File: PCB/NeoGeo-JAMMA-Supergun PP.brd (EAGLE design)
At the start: 58.5 x 61 mm, 18 parts, among them U1A SN74AHCT125N, U2A SN74AHCT125N, U3A SN74AHCT125N

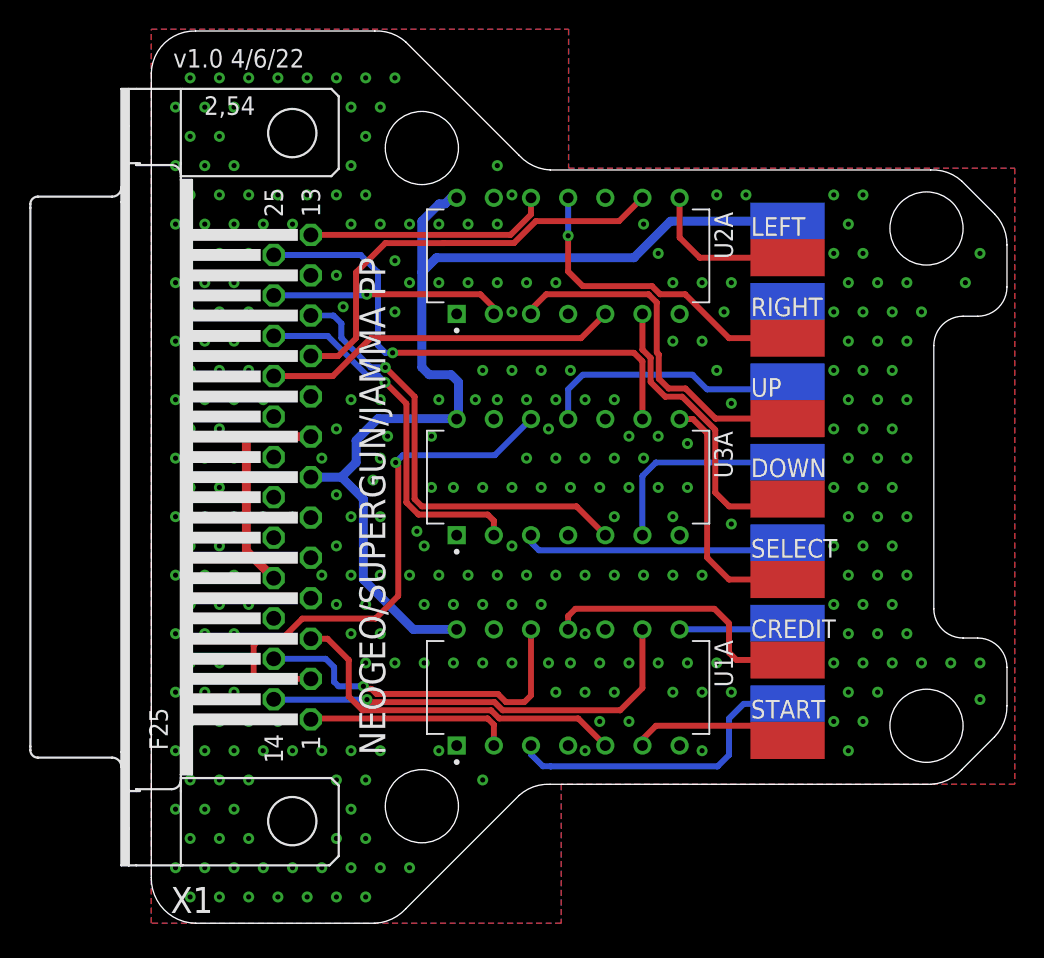
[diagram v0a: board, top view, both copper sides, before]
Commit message: Added exposed GND plane at DB25 anchors
All PCBs have been update to have exposed GND plane pads for the DB25 anchor points.

This resolves Issue 54
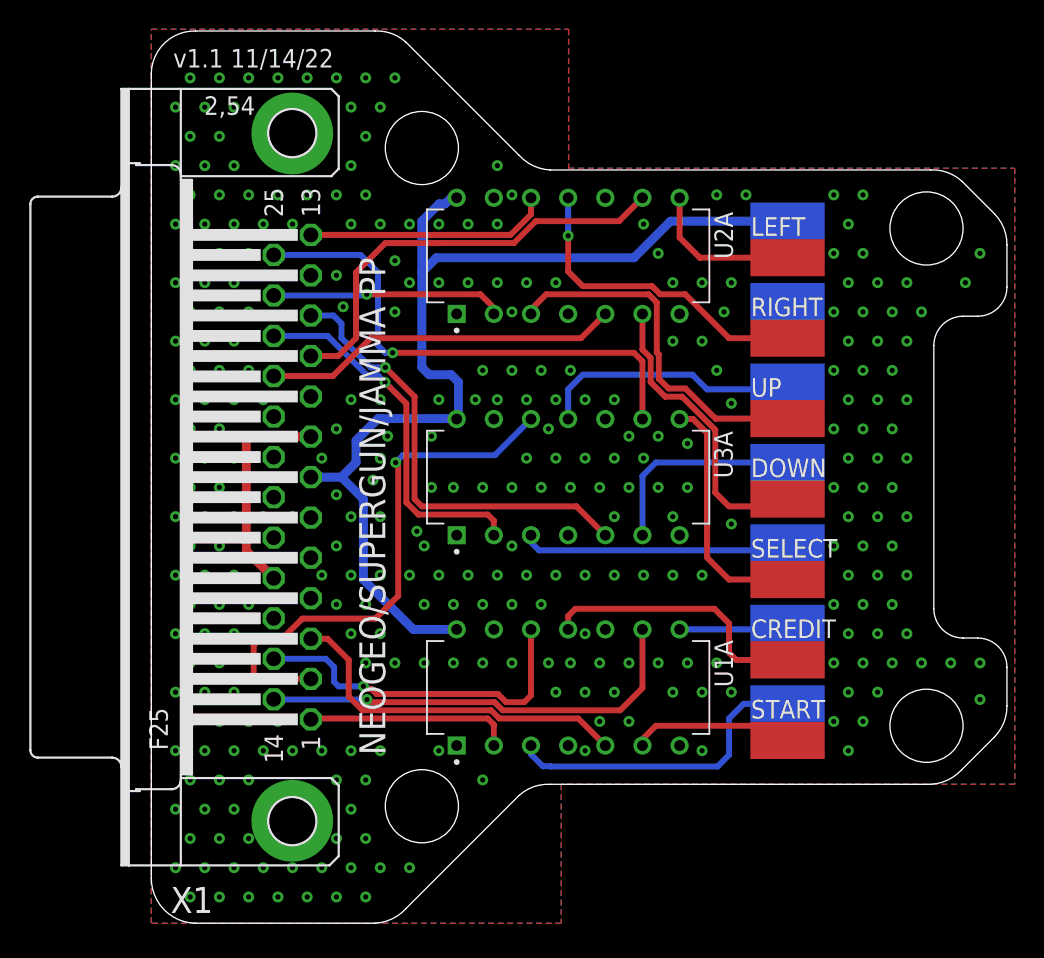
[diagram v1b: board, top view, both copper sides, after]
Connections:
- net GND: now also X1.P$1, X1.P$2
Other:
- board text added: "v1.1 11/14/22"
- board text removed: "v1.0 4/6/22"
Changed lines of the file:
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@@
 <hole x="18.5" y="53" drill="5"/>
 <hole x="18.5" y="8" drill="5"/>
-<text x="1.5" y="58.5" size="1.27" layer="21">v1.0 4/6/22</text>
+<text x="1.5" y="58.5" size="1.27" layer="21">v1.1 11/14/22</text>
 <text x="16" y="11.5" size="1.778" layer="21" rot="R90">NEOGEO/SUPERGUN/JAMMA PP</text>
 <wire x1="58.5" y1="46.377359375" x2="58.5" y2="43.5" width="0" layer="20"/>
@@
 <contactref element="U2A" pad="1"/>
 <contactref element="GND" pad="1"/>
-<contactref element="X1" pad="9"/>
-<contactref element="X1" pad="6"/>
-<contactref element="X1" pad="5"/>
-<contactref element="X1" pad="4"/>
-<contactref element="X1" pad="16"/>
 <via x="2.6568" y="1.7968" extent="1-16" drill="0.35"/>
 <via x="1.6568" y="3.7968" extent="1-16" drill="0.35"/>
@@
 <via x="55.6568" y="43.7968" extent="1-16" drill="0.35"/>
 <via x="56.6568" y="45.7968" extent="1-16" drill="0.35"/>
+<contactref element="X1" pad="9"/>
+<contactref element="X1" pad="6"/>
+<contactref element="X1" pad="5"/>
+<contactref element="X1" pad="4"/>
+<contactref element="X1" pad="16"/>
+<contactref element="X1" pad="P$1"/>
+<contactref element="X1" pad="P$2"/>
+<wire x1="8.6568" y1="57.7968" x2="9.64" y2="53.995" width="0" layer="19" extent="1-1"/>
+<wire x1="9.64" y1="7.005" x2="9.6568" y2="3.7968" width="0" layer="19" extent="1-1"/>
 </signal>
 <signal name="5VIN">

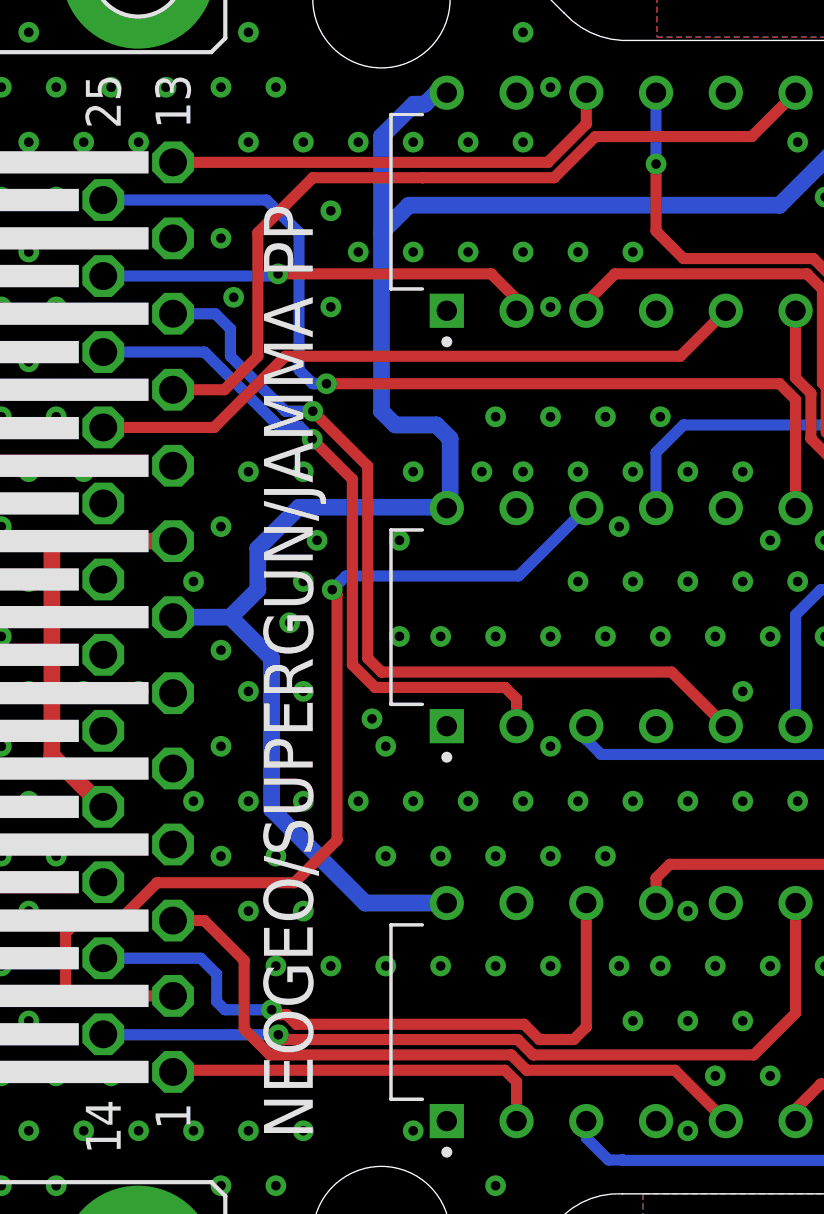
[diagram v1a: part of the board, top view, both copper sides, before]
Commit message: Silkscreen Update, Library Add, Datasheet Add
Updated the silkscreen on all PCBs that used the SN74 components as there was not orientation marker on the silkscreen.

Added Modified SN74 libraries and VB Cable Pinout image
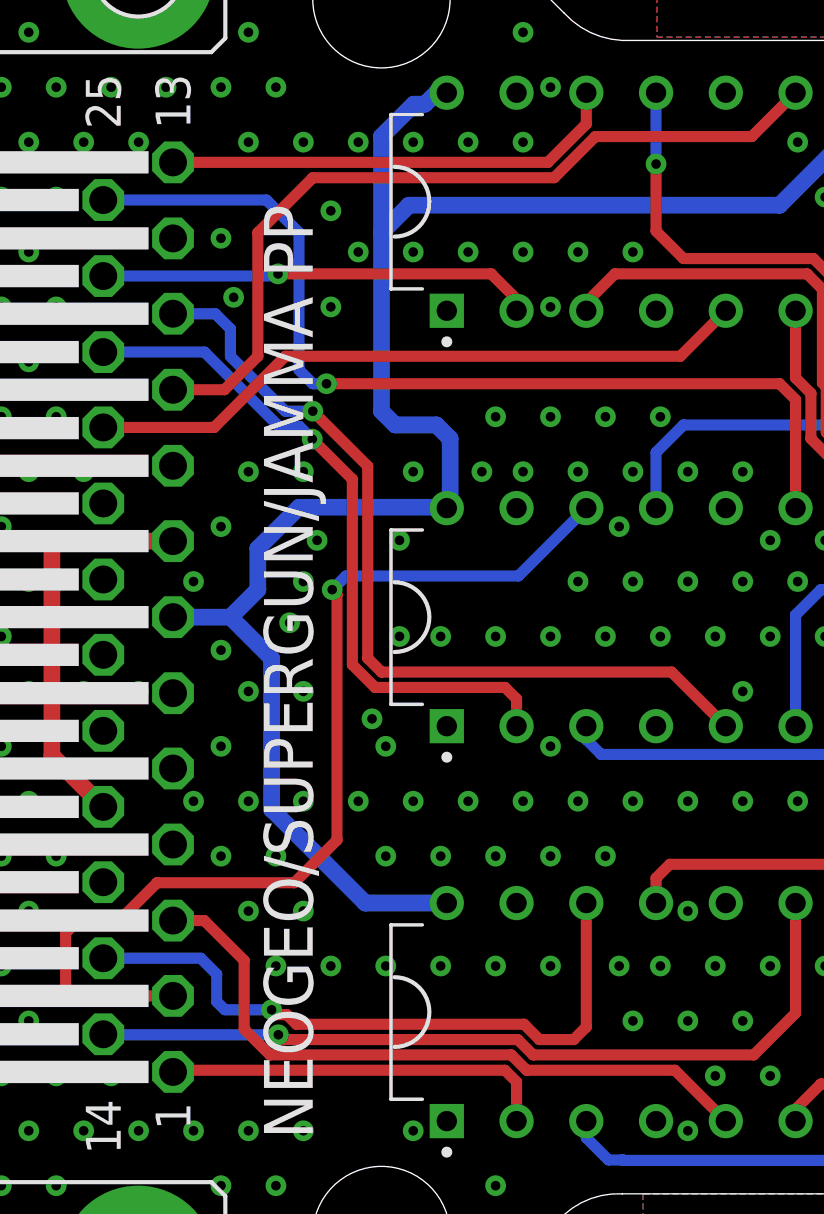
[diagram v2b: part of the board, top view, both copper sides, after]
